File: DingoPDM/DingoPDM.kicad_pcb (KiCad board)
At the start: 4 copper layers, 72.4 x 95.2 mm, 148 parts, among them J1 RedCubeTerminal, J2 RedCubeTerminal, J3 Conn_01x12, J4 TC, J5 USB_C_Receptacle_USB2.0, SW1 BOOT, U1 VXO780x-500-M, U10 BTS7008-2EPA, U11 BTS7008-2EPA, U12 LM324, U13 BTS7008-2EPA, U2 LD1117S33CTR, U3 PCA82C250, U4 STM32F446RETx, U5 MB85RC256V, U6 MCP9808, U7 LM324, U8 BTS700n-1EPP, U9 BTS700n-1EPP, Y1 8mHz

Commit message: Status and Error LED part num switched
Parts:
- D16: value GRN -> RED
- D17: value RED -> GRN
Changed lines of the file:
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@@
     (descr "LED SMD 0805 (2012 Metric), square (rectangular) end terminal, IPC_7351 nominal, (Body size source: https://docs.google.com/spreadsheets/d/1BsfQQcO9C6DZCsRaXUlFlo91Tg2WpOkGARC1WS5S8t0/edit?usp=sharing), generated with kicad-footprint-generator")
     (tags "LED")
-    (property "Digi-Key_PN" "475-1278-1-ND")
-    (property "LCSC" "C2899997")
+    (property "Digi-Key_PN" "475-1410-1-ND")
+    (property "LCSC" "C2899888")
     (property "Sheetfile" "MCU.kicad_sch")
     (property "Sheetname" "MCU")
@@
         (effects (font (size 1 1) (thickness 0.15)))
     )
-    (fp_text value "RED" (at 0 1.65) (layer "F.Fab") hide
+    (fp_text value "GRN" (at 0 1.65) (layer "F.Fab") hide
         (effects (font (size 1 1) (thickness 0.15)))
     )
@@
     (descr "LED SMD 0805 (2012 Metric), square (rectangular) end terminal, IPC_7351 nominal, (Body size source: https://docs.google.com/spreadsheets/d/1BsfQQcO9C6DZCsRaXUlFlo91Tg2WpOkGARC1WS5S8t0/edit?usp=sharing), generated with kicad-footprint-generator")
     (tags "LED")
-    (property "Digi-Key_PN" "475-1410-1-ND")
-    (property "LCSC" "C2899888")
+    (property "Digi-Key_PN" "475-1278-1-ND")
+    (property "LCSC" "C2899997")
     (property "Sheetfile" "MCU.kicad_sch")
     (property "Sheetname" "MCU")
@@
         (effects (font (size 1 1) (thickness 0.15)))
     )
-    (fp_text value "GRN" (at 0 1.65) (layer "F.Fab") hide
-        (effects (font (size 1 1) (thickness 0.15)))
-    )
+    (fp_text value "RED" (at 0 1.65) (layer "F.Fab") hide
+        (effects (font (size 1 1) (thickness 0.15)))
+    )

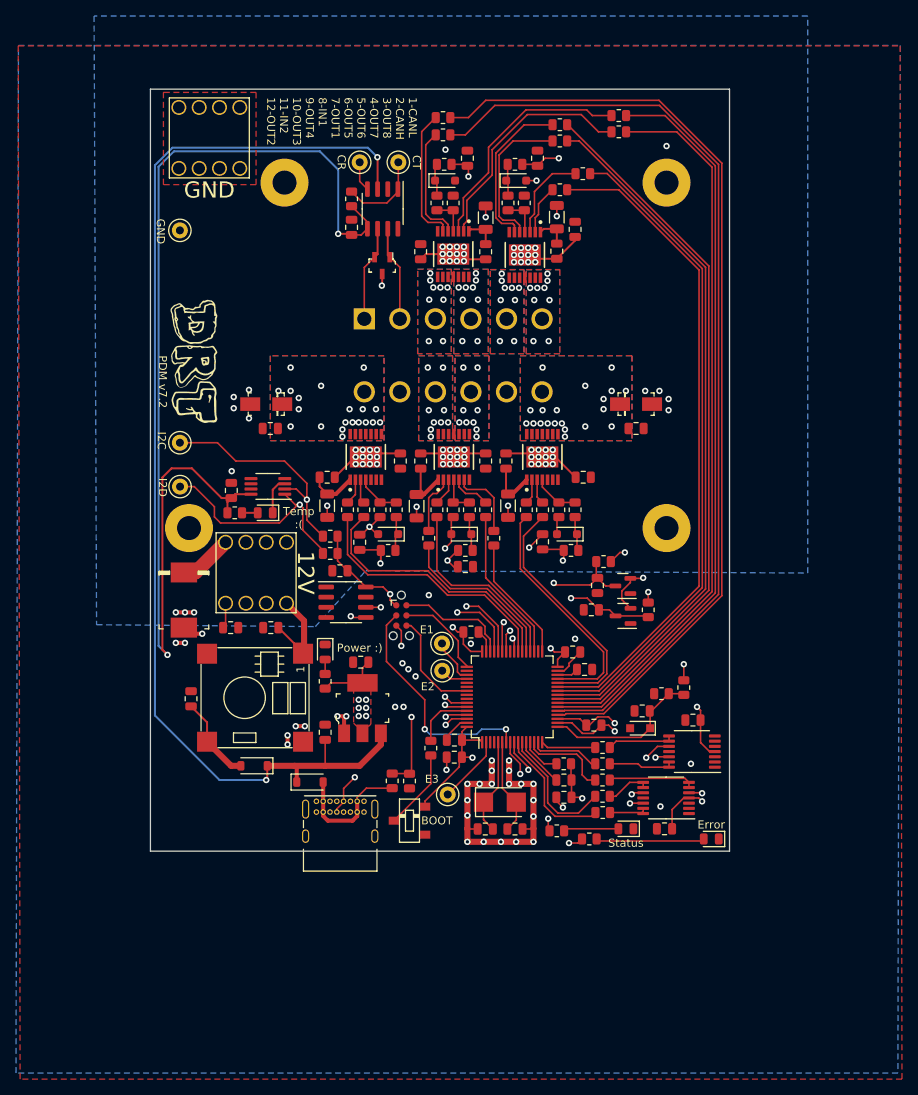
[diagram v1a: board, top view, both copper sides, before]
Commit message: Fixed USB, power LED and CAN standby
And increased screw hole size
#9, #11, #12, #13
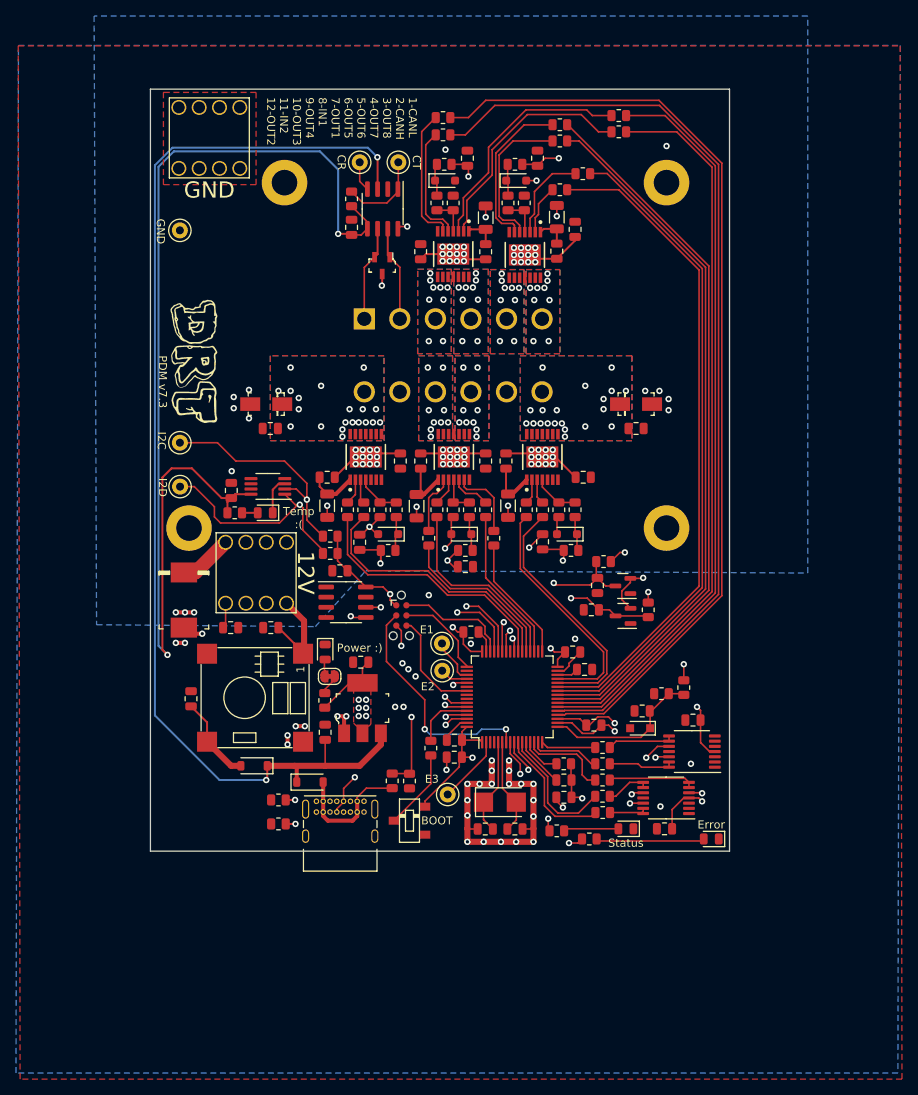
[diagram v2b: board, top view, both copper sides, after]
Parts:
- added JP1: PowerLED_Jumper, Jumper:SolderJumper-2_P1.3mm_Bridged_RoundedPad1.0x1.5mm, F.Cu at (-15.4, 40.1)
- added R54: 5.1K, Resistor_SMD:R_0805_2012Metric, F.Cu at (-21.8, 58.6)
- added R55: 5.1K, Resistor_SMD:R_0805_2012Metric, F.Cu at (-21.8, 55.6)
- H1, H2, H3, H4: footprint MountingHole:MountingHole_3mm_Pad -> MountingHole:MountingHole_3.2mm_M3_ISO7380_Pad
- R2: value 10K -> 4.7K
- moved R3 2.39 mm to (-16.1, 43.1)
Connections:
- J5 pad A5: unconnected-(J5-CC1-PadA5) -> Net-(J5-CC1)
- J5 pad B5: unconnected-(J5-CC2-PadB5) -> Net-(J5-CC2)
- R3 pad 1: Net-(D3-A) -> Net-(JP1-B)
- U3 pad 8: GND -> /MCU/CAN_STANDBY
- U4 pad 53: unconnected-(U4-PC12-Pad53) -> /MCU/CAN_STANDBY
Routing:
- net /MCU/CAN_STANDBY: track 0.00 -> 92.6 mm, vias 0 -> 2
- net Net-(J5-CC2): track 0.00 -> 8.99 mm, vias 0 -> 1
- net Net-(J5-CC1): track 0.00 -> 6.48 mm, vias 0 -> 1
- net Net-(JP1-B): track 0.00 -> 2.61 mm
- net +3V3: track 220.2 -> 221.3 mm
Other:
- board text added: "PDM v7.3"
- board text removed: "PDM v7.2"

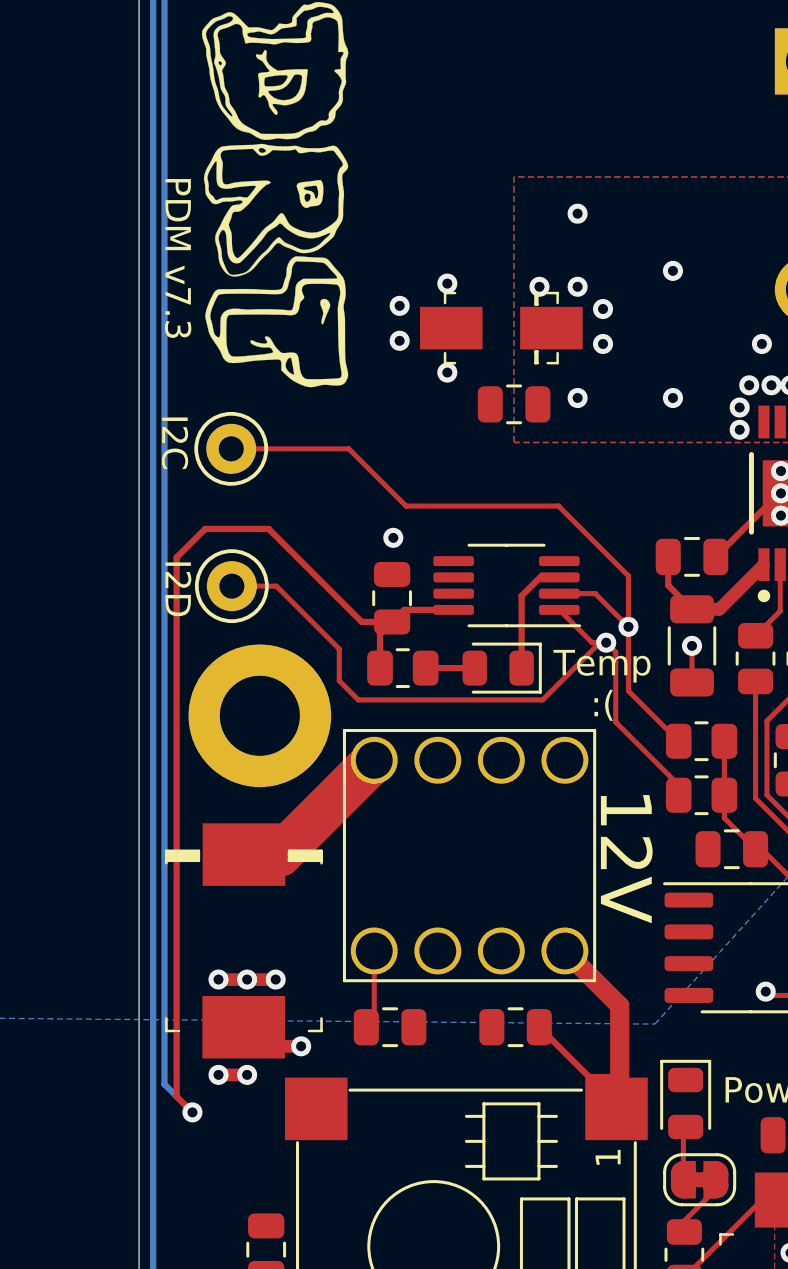
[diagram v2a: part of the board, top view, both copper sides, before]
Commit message: Added diode for reverse battery protection
#14
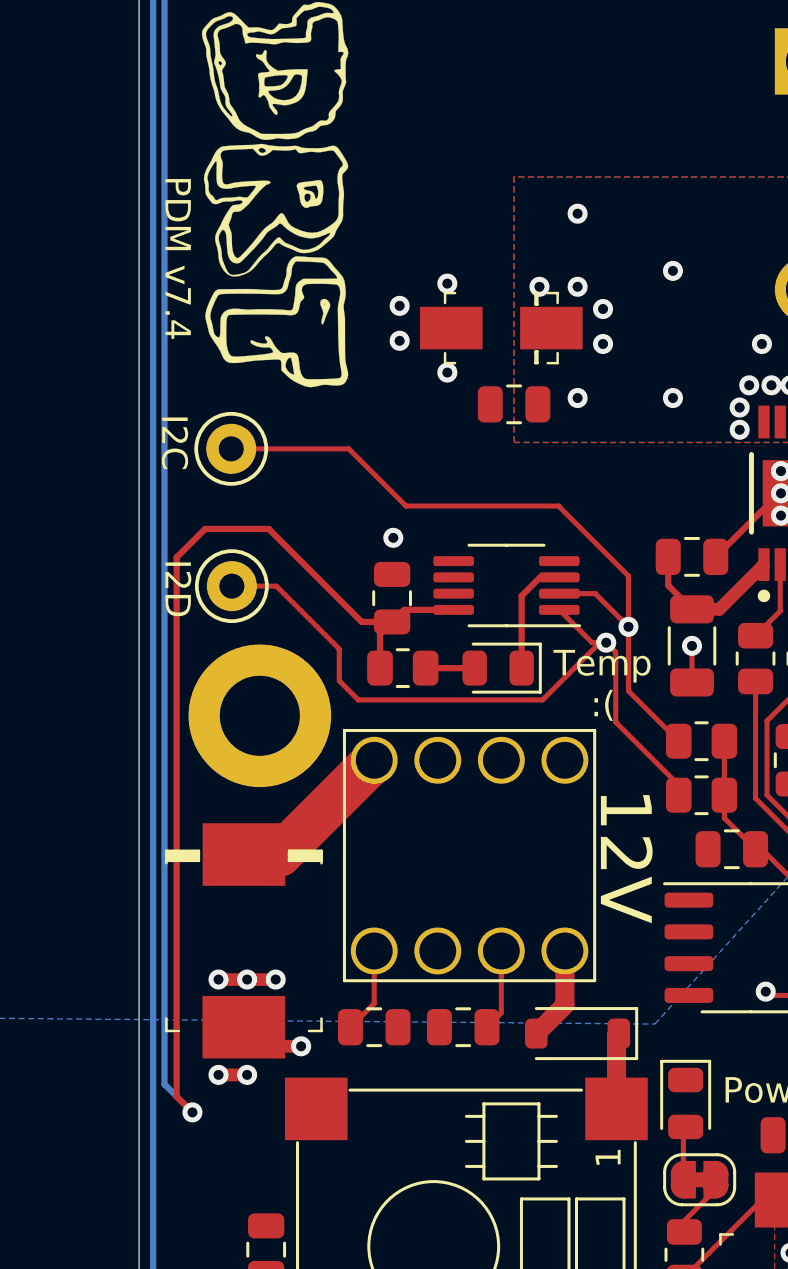
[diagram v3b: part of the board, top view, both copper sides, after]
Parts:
- added D19: Schottky, Diode_SMD:D_SOD-123, F.Cu at (-20.3, 34.3)
- moved C3 2.09 mm to (-24.9, 34.0)
- moved C2 0.64 mm to (-28.4, 34.0)
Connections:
- U1 pad 1: +12V -> Net-(D19-K)
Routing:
- net Net-(D19-K): track 0.00 -> 3.05 mm
- net +12V: track 99.9 -> 97.3 mm
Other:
- board text added: "PDM v7.4"
- board text removed: "PDM v7.3"
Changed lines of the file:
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@@
   (net 136 "Net-(J5-CC1)")
   (net 137 "Net-(J5-CC2)")
+  (net 138 "Net-(D19-K)")
   (footprint "Resistor_SMD:R_0805_2012Metric" (layer "F.Cu")
     (at 11.176 19.304 -90)
@@
       (stroke (width 0.12) (type solid)) (fill none) (layer "F.SilkS"))
     (pad "1" smd rect (at -5.5 -6 270) (size 2.5 2.5) (layers "F.Cu" "F.Paste" "F.Mask")
-      (net 5 "+12V") (pinfunction "VIN") (pintype "power_in"))
+      (net 138 "Net-(D19-K)") (pinfunction "VIN") (pintype "power_in"))
     (pad "2" smd rect (at 5.5 -6 270) (size 2.5 2.5) (layers "F.Cu" "F.Paste" "F.Mask")
       (net 1 "GND") (pinfunction "GND") (pintype "power_in"))
@@
   )
   (footprint "Capacitor_SMD:C_0805_2012Metric" (layer "F.Cu")
-    (at -27.813 34.036)
+    (at -28.448 34.036)
     (descr "Capacitor SMD 0805 (2012 Metric), square (rectangular) end terminal, IPC_7351 nominal, (Body size source: IPC-SM-782 page 76, https://www.pcb-3d.com/wordpress/wp-content/uploads/ipc-sm-782a_amendment_1_and_2.pdf, https://docs.google.com/spreadsheets/d/1BsfQQcO9C6DZCsRaXUlFlo91Tg2WpOkGARC1WS5S8t0/edit?usp=sharing), generated with kicad-footprint-generator")
     (tags "capacitor")
@@
   )
   (footprint "Capacitor_SMD:C_0805_2012Metric" (layer "F.Cu")
-    (at -22.799 34.036 180)
+    (at -24.892 34.036 180)
     (descr "Capacitor SMD 0805 (2012 Metric), square (rectangular) end terminal, IPC_7351 nominal, (Body size source: IPC-SM-782 page 76, https://www.pcb-3d.com/wordpress/wp-content/uploads/ipc-sm-782a_amendment_1_and_2.pdf, https://docs.google.com/spreadsheets/d/1BsfQQcO9C6DZCsRaXUlFlo91Tg2WpOkGARC1WS5S8t0/edit?usp=sharing), generated with kicad-footprint-generator")
     (tags "capacitor")
@@
     )
   )
+  (footprint "Diode_SMD:D_SOD-123" (layer "F.Cu")
+    (at -20.32 34.29 180)
+    (descr "SOD-123")
+    (tags "SOD-123")
+    (property "Digi-Key_PN" "1727-2394-1-ND")
+    (property "LCSC" "C179426")
+    (property "Sheetfile" "Power.kicad_sch")
+    (property "Sheetname" "Power")
+    (property "ki_description" "Schottky diode")
+    (property "ki_keywords" "diode Schottky")
+    (attr smd)
+    (fp_text reference "D19" (at 0 -2) (layer "F.SilkS") hide
+        (effects (font (size 1 1) (thickness 0.15)))
+    )
+    (fp_text value "Schottky" (at 0 2.1) (layer "F.Fab") hide
+        (effects (font (size 1 1) (thickness 0.15)))
+    )
+    (fp_text user "${REFERENCE}" (at 0 -2) (layer "F.Fab") hide
+        (effects (font (size 1 1) (thickness 0.15)))
+    )
+    (fp_line (start -2.36 -1) (end -2.36 1)
+      (stroke (width 0.12) (type solid)) (layer "F.SilkS"))
+    (fp_line (start -2.36 -1) (end 1.65 -1)
+      (stroke (width 0.12) (type solid)) (layer "F.SilkS"))
+    (fp_line (start -2.36 1) (end 1.65 1)
+      (stroke (width 0.12) (type solid)) (layer "F.SilkS"))
+    (fp_line (start -2.35 -1.15) (end -2.35 1.15)
+      (stroke (width 0.05) (type solid)) (layer "F.CrtYd"))
+    (fp_line (start -2.35 -1.15) (end 2.35 -1.15)
+      (stroke (width 0.05) (type solid)) (layer "F.CrtYd"))
+    (fp_line (start 2.35 -1.15) (end 2.35 1.15)
+      (stroke (width 0.05) (type solid)) (layer "F.CrtYd"))
+    (fp_line (start 2.35 1.15) (end -2.35 1.15)
+      (stroke (width 0.05) (type solid)) (layer "F.CrtYd"))
+    (fp_line (start -1.4 -0.9) (end 1.4 -0.9)
+      (stroke (width 0.1) (type solid)) (layer "F.Fab"))
+    (fp_line (start -1.4 0.9) (end -1.4 -0.9)
+      (stroke (width 0.1) (type solid)) (layer "F.Fab"))
+    (fp_line (start -0.75 0) (end -0.35 0)
+      (stroke (width 0.1) (type solid)) (layer "F.Fab"))
+    (fp_line (start -0.35 0) (end -0.35 -0.55)
+      (stroke (width 0.1) (type solid)) (layer "F.Fab"))
+    (fp_line (start -0.35 0) (end -0.35 0.55)
+      (stroke (width 0.1) (type solid)) (layer "F.Fab"))
+    (fp_line (start -0.35 0) (end 0.25 -0.4)
+      (stroke (width 0.1) (type solid)) (layer "F.Fab"))
+    (fp_line (start 0.25 -0.4) (end 0.25 0.4)
+      (stroke (width 0.1) (type solid)) (layer "F.Fab"))
+    (fp_line (start 0.25 0) (end 0.75 0)
+      (stroke (width 0.1) (type solid)) (layer "F.Fab"))
+    (fp_line (start 0.25 0.4) (end -0.35 0)
+      (stroke (width 0.1) (type solid)) (layer "F.Fab"))
+    (fp_line (start 1.4 -0.9) (end 1.4 0.9)
+      (stroke (width 0.1) (type solid)) (layer "F.Fab"))
+    (fp_line (start 1.4 0.9) (end -1.4 0.9)
+      (stroke (width 0.1) (type solid)) (layer "F.Fab"))
+    (pad "1" smd roundrect (at -1.65 0 180) (size 0.9 1.2) (layers "F.Cu" "F.Paste" "F.Mask") (roundrect_rratio 0.25)
+      (net 138 "Net-(D19-K)") (pinfunction "K") (pintype "passive"))
+    (pad "2" smd roundrect (at 1.65 0 180) (size 0.9 1.2) (layers "F.Cu" "F.Paste" "F.Mask") (roundrect_rratio 0.25)
+      (net 5 "+12V") (pinfunction "A") (pintype "passive"))
+    (model "${KICAD6_3DMODEL_DIR}/Diode_SMD.3dshapes/D_SOD-123.wrl"
+      (offset (xyz 0 0 0))
+      (scale (xyz 1 1 1))
+      (rotate (xyz 0 0 0))
+    )
+  )
   (footprint "Connector:Tag-Connect_TC2030-IDC-NL_2x03_P1.27mm_Vertical" (layer "F.Cu")
     (at -6.477 32.512 -90)
@@
     (effects (font (size 1.016 1.016) (thickness 0.1524)))
   )
-  (gr_text "PDM v7.3" (at -36.322 3.302 270) (layer "F.SilkS")
+  (gr_text "PDM v7.4" (at -36.322 3.302 270) (layer "F.SilkS")
     (effects (font (size 1.016 1.016) (thickness 0.1524)))
   )
@@
   (segment (start 0.614625 26.9748) (end 15.6718 26.9748) (width 0.2032) (layer "In2.Cu") (net 4))
   (segment (start 6.604 12.258) (end 10.7028 12.258) (width 0.25) (layer "F.Cu") (net 5))
-  (segment (start -28.448 33.721) (end -28.448 30.988) (width 0.2032) (layer "F.Cu") (net 5))
   (segment (start 12.954 -12.07) (end 9.8502 -12.07) (width 0.25) (layer "F.Cu") (net 5))
   (segment (start 12.954 -12.07) (end 15.24 -14.356) (width 0.25) (layer "F.Cu") (net 5))
+  (segment (start -20.828 33.148) (end -21.97 34.29) (width 0.762) (layer "F.Cu") (net 5))
+  (segment (start -28.448 33.086) (end -28.448 30.988) (width 0.2032) (layer "F.Cu") (net 5))
   (segment (start -6.604 12.258) (end -8.951 12.258) (width 0.25) (layer "F.Cu") (net 5))
   (segment (start -10.287 12.7) (end -10.287 11.811) (width 0.25) (layer "F.Cu") (net 5))
   (segment (start -33.655 27.136) (end -32.216 27.136) (width 1.7526) (layer "F.Cu") (net 5))
   (segment (start -0.36 12.258) (end 0.082 12.7) (width 0.25) (layer "F.Cu") (net 5))
+  (segment (start -23.368 33.462) (end -23.368 30.988) (width 0.2032) (layer "F.Cu") (net 5))
   (segment (start -12.065 12.7) (end -12.258 12.7) (width 0.25) (layer "F.Cu") (net 5))
+  (segment (start -29.398 34.036) (end -28.448 33.086) (width 0.2032) (layer "F.Cu") (net 5))
   (segment (start -10.922 12.7) (end -11.176 12.7) (width 0.25) (layer "F.Cu") (net 5))
   (segment (start -9.845 12.258) (end -10.287 12.7) (width 0.25) (layer "F.Cu") (net 5))
   (segment (start 0.524 12.258) (end 0.082 12.7) (width 0.25) (layer "F.Cu") (net 5))
   (segment (start -8.951 12.258) (end -9.398 11.811) (width 0.25) (layer "F.Cu") (net 5))
-  (segment (start -19.856 36.029) (end -18.638 36.029) (width 0.25) (layer "F.Cu") (net 5))
   (segment (start -10.287 11.811) (end -10.48 12.258) (width 0.25) (layer "F.Cu") (net 5))
   (segment (start 10.7028 12.258) (end 11.1448 12.7) (width 0.25) (layer "F.Cu") (net 5))
-  (segment (start -18.638 36.029) (end -18.638 33.178) (width 0.762) (layer "F.Cu") (net 5))
-  (segment (start -28.763 34.036) (end -28.448 33.721) (width 0.2032) (layer "F.Cu") (net 5))
   (segment (start -32.216 27.136) (end -28.448 23.368) (width 1.7526) (layer "F.Cu") (net 5))
   (segment (start -10.48 12.258) (end -10.922 12.7) (width 0.25) (layer "F.Cu") (net 5))
@@
   (segment (start 28.829 40.6165) (end 28.829 38.608) (width 0.2032) (layer "F.Cu") (net 5))
   (segment (start 4.064 -12.004) (end 0.2388 -12.004) (width 0.25) (layer "F.Cu") (net 5))
+  (segment (start -20.828 30.988) (end -20.828 33.148) (width 0.762) (layer "F.Cu") (net 5))
   (segment (start 15.306 15.24) (end 12.766 12.7) (width 0.25) (layer "F.Cu") (net 5))
   (segment (start 0.2388 -12.004) (end -0.4318 -12.6746) (width 0.25) (layer "F.Cu") (net 5))
-  (segment (start -21.849 34.036) (end -19.856 36.029) (width 0.25) (layer "F.Cu") (net 5))
   (segment (start -3.4136 -12.6544) (end 0.0104 -12.6544) (width 0.25) (layer "F.Cu") (net 5))
+  (segment (start -23.942 34.036) (end -23.368 33.462) (width 0.2032) (layer "F.Cu") (net 5))
   (segment (start 12.766 12.7) (end 11.1448 12.7) (width 0.25) (layer "F.Cu") (net 5))
-  (segment (start -18.638 33.178) (end -20.828 30.988) (width 0.762) (layer "F.Cu") (net 5))
   (segment (start 9.8502 -12.07) (end 9.3726 -12.5476) (width 0.25) (layer "F.Cu") (net 5))
   (segment (start -12.258 12.7) (end -14.798 15.24) (width 0.25) (layer "F.Cu") (net 5))
@@
   (segment (start -13.833626 58.5724) (end -19.7104 58.5724) (width 0.25) (layer "In2.Cu") (net 137))
   (segment (start -12.8474 57.586174) (end -13.833626 58.5724) (width 0.25) (layer "In2.Cu") (net 137))
+  (segment (start -18.765 34.385) (end -18.67 34.29) (width 0.762) (layer "F.Cu") (net 138))
+  (segment (start -18.765 37.299) (end -18.765 34.385) (width 0.762) (layer "F.Cu") (net 138))
   (zone (net 20) (net_name "+3V3") (layer "F.Cu") (hatch edge 0.5)
     (priority 8)
